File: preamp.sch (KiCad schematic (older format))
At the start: 1 part

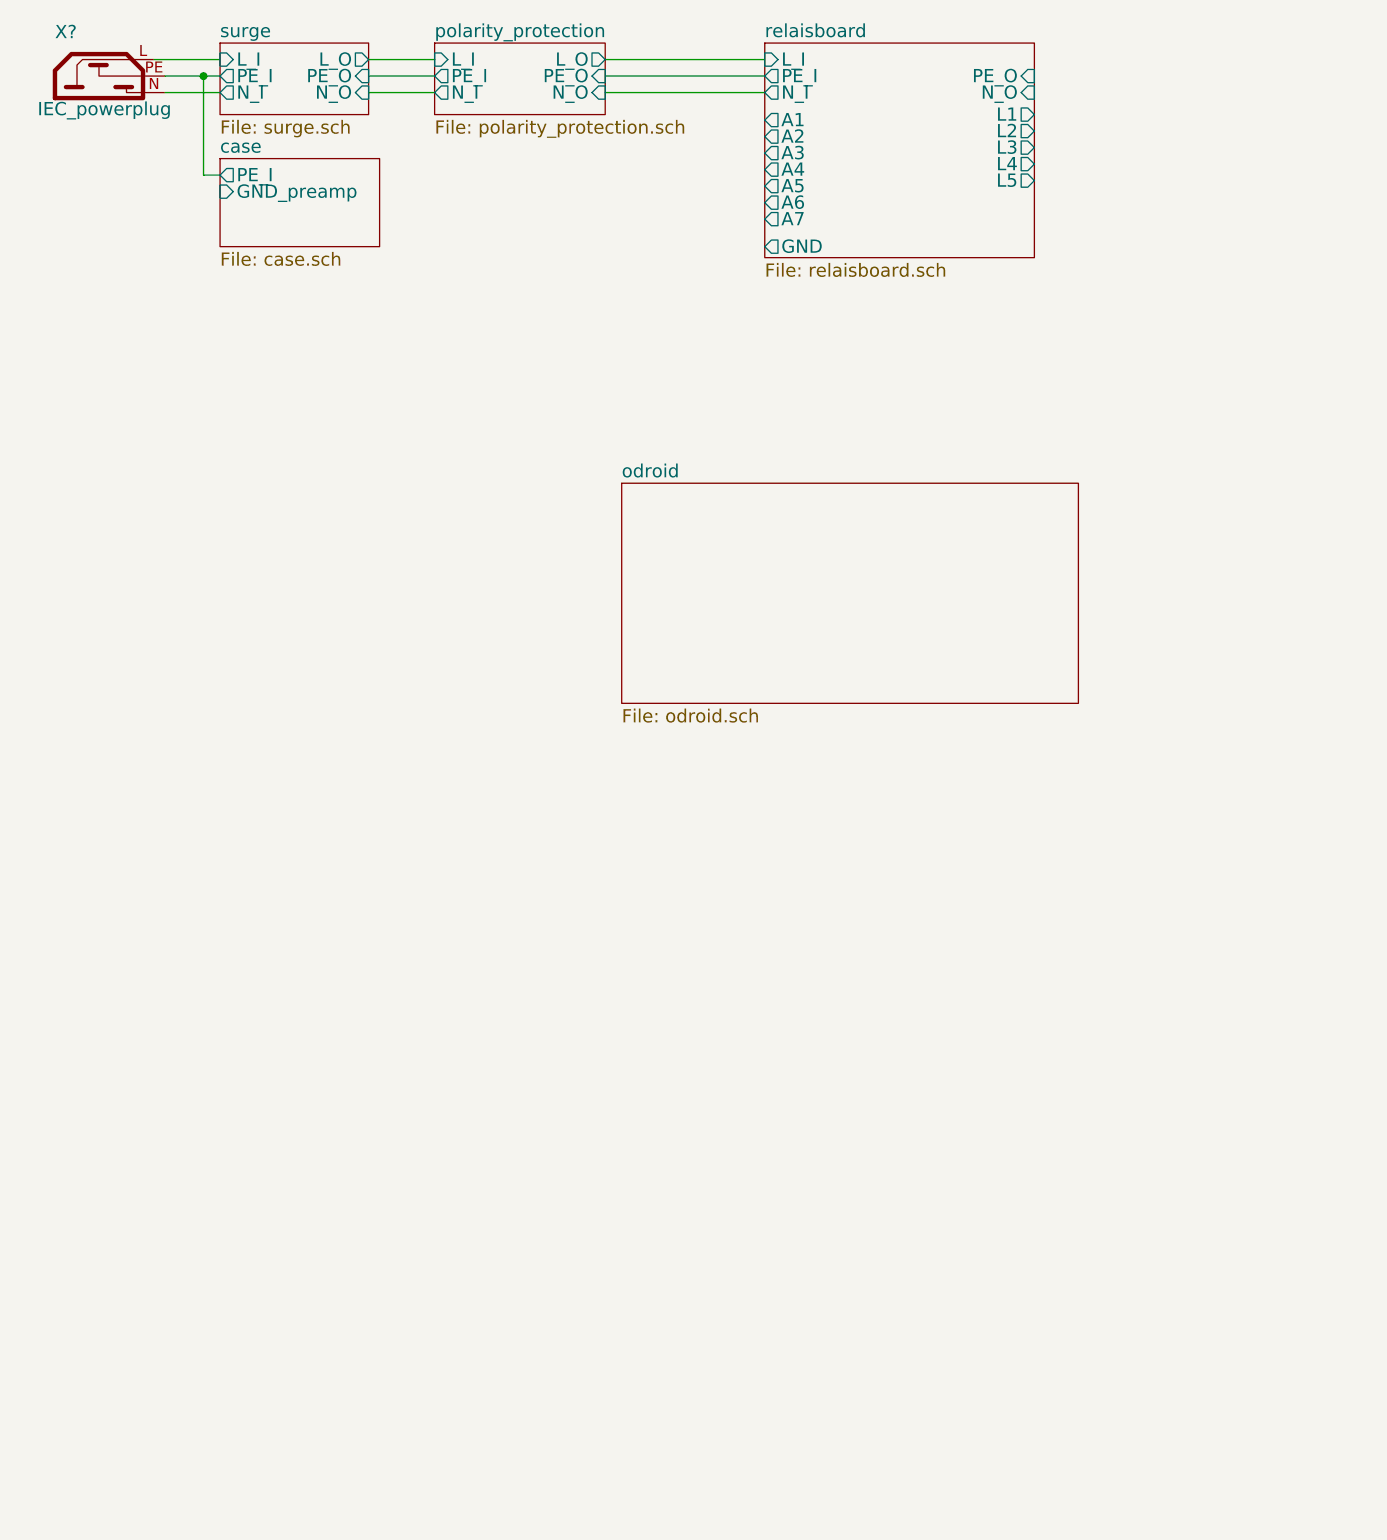
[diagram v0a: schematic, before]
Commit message: toslink reciever and transmitter
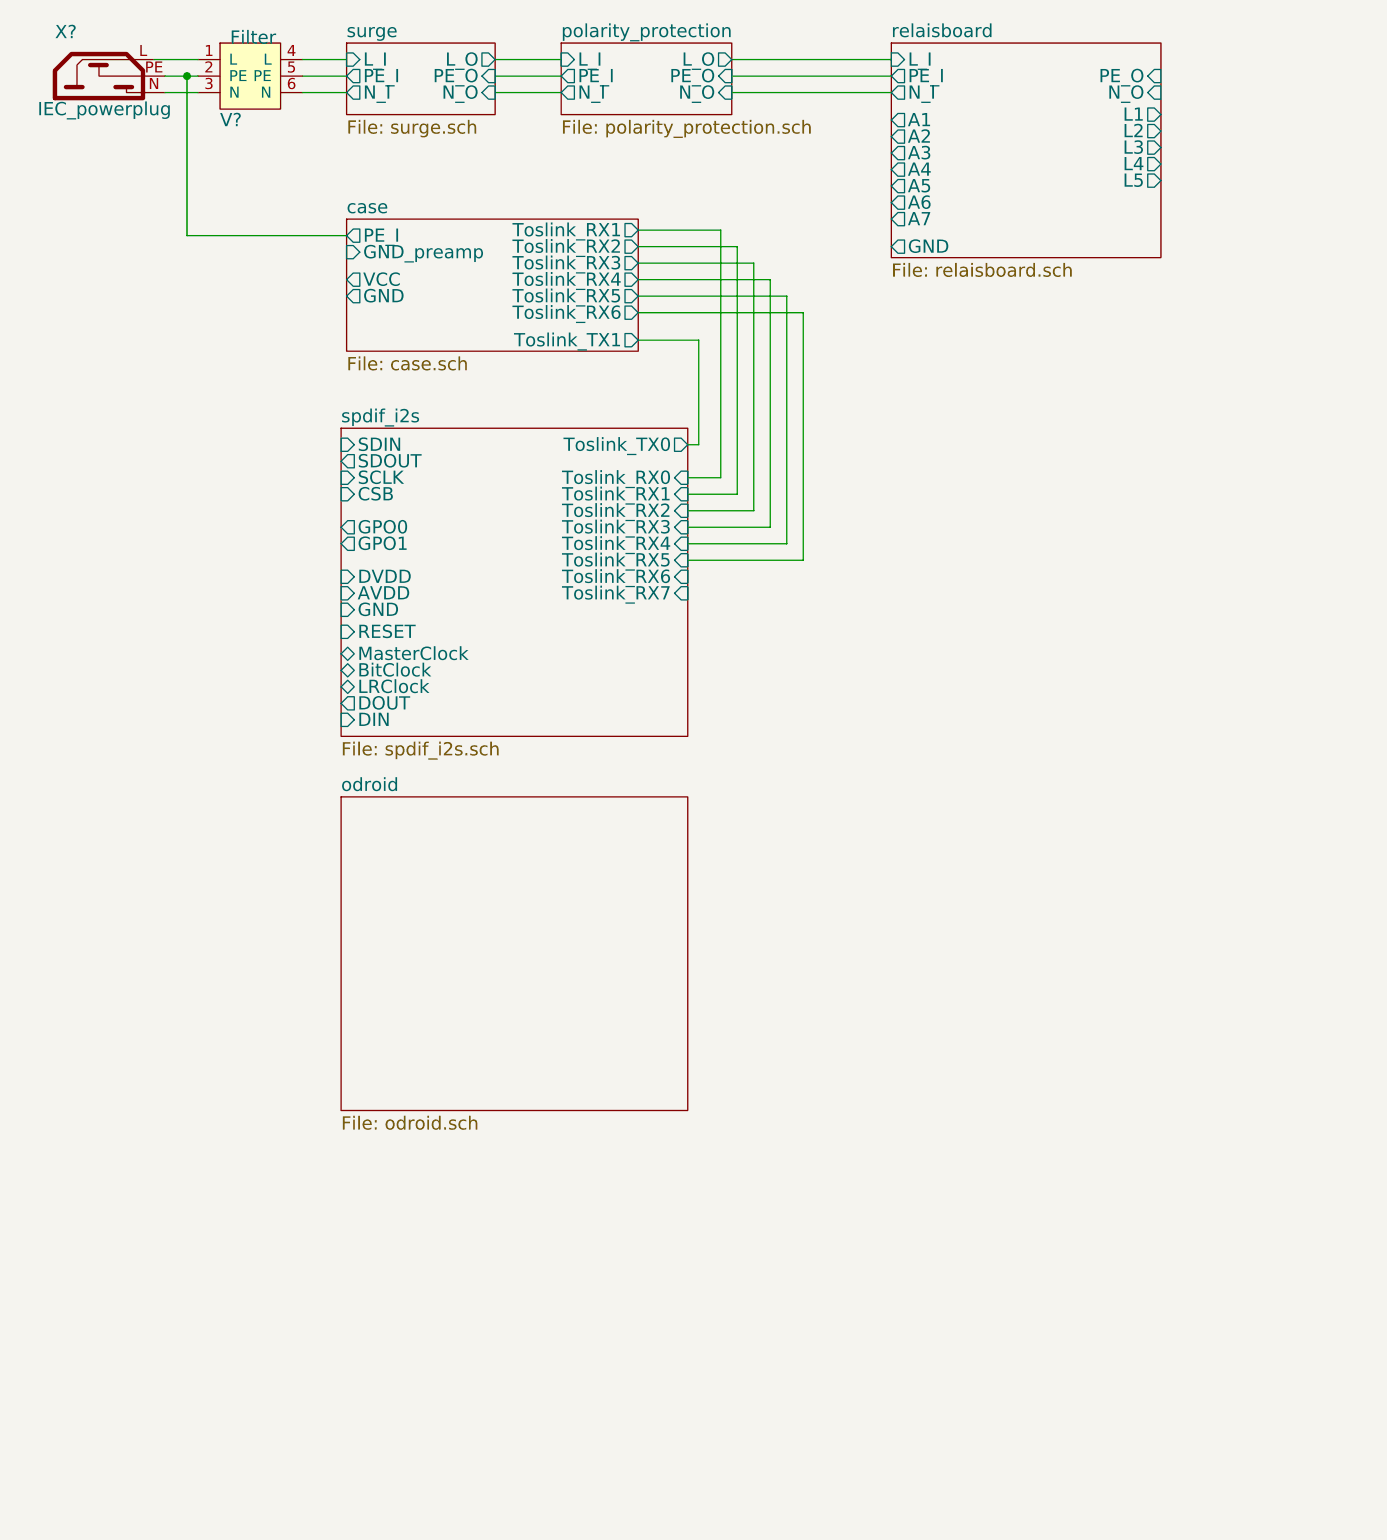
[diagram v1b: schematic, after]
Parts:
- added V?: Filter, symbol Filter
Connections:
- net case/PE_I: now also V?.2 (PE)
- net surge/L_I: now also V?.4 (L); no longer X?.L
- net surge/N_I: now also V?.6 (N); no longer X?.N
- new net: V?.1 (L), X?.L
- new net: V?.3 (N), X?.N
- new net surge/PE_I: V?.5 (PE)
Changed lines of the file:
@@
 $Descr A4 11693 8268
 encoding utf-8
-Sheet 1 6
+Sheet 1 7
 Title ""
 Date ""
@@
 $EndDescr
 $Sheet
-S 1425 825  675  325
+S 2000 825  675  325
 U 5882A13F
 F0 "surge" 60
 F1 "surge.sch" 60
-F2 "L_I" I L 1425 900 60
-F3 "PE_I" O L 1425 975 60
-F4 "N_I" O L 1425 1050 60
-F5 "L_O" O R 2100 900 60
-F6 "PE_O" I R 2100 975 60
-F7 "N_O" I R 2100 1050 60
+F2 "L_I" I L 2000 900 60
+F3 "PE_I" O L 2000 975 60
+F4 "N_I" O L 2000 1050 60
+F5 "L_O" O R 2675 900 60
+F6 "PE_O" I R 2675 975 60
+F7 "N_O" I R 2675 1050 60
 $EndSheet
 $Comp
@@
 	1    0    0    -1
 $EndComp
-Wire Wire Line
-	1125 900  1425 900
-Wire Wire Line
-	1175 975  1425 975
-Wire Wire Line
-	1175 1050 1425 1050
-$Sheet
-S 2400 825  775  325
+$Sheet
+S 2975 825  775  325
 U 58836B99
 F0 "polarity_protection" 60
 F1 "polarity_protection.sch" 60
-F2 "L_I" I L 2400 900 60
-F3 "PE_I" O L 2400 975 60
-F4 "N_I" O L 2400 1050 60
-F5 "L_O" O R 3175 900 60
-F6 "PE_O" I R 3175 975 60
-F7 "N_O" I R 3175 1050 60
-$EndSheet
-Wire Wire Line
-	2100 900  2400 900
-Wire Wire Line
-	2400 975  2100 975
-Wire Wire Line
-	2100 1050 2400 1050
-$Sheet
-S 3900 825  1225 975
+F2 "L_I" I L 2975 900 60
+F3 "PE_I" O L 2975 975 60
+F4 "N_I" O L 2975 1050 60
+F5 "L_O" O R 3750 900 60
+F6 "PE_O" I R 3750 975 60
+F7 "N_O" I R 3750 1050 60
+$EndSheet
+Wire Wire Line
+	2675 900  2975 900
+Wire Wire Line
+	2975 975  2675 975
+Wire Wire Line
+	2675 1050 2975 1050
+$Sheet
+S 4475 825  1225 975
 U 58838AD0
 F0 "relaisboard" 60
 F1 "relaisboard.sch" 60
-F2 "L_I" I L 3900 900 60
-F3 "PE_I" O L 3900 975 60
-F4 "N_I" O L 3900 1050 60
-F5 "PE_O" I R 5125 975 60
-F6 "N_O" I R 5125 1050 60
-F7 "L1" O R 5125 1150 60
-F8 "L2" O R 5125 1225 60
-F9 "L3" O R 5125 1300 60
-F10 "L4" O R 5125 1375 60
-F11 "L5" O R 5125 1450 60
-F12 "GND" O L 3900 1750 60
-F13 "A1" O L 3900 1175 60
-F14 "A2" O L 3900 1250 60
-F15 "A3" O L 3900 1325 60
-F16 "A4" O L 3900 1400 60
-F17 "A5" O L 3900 1475 60
-F18 "A6" O L 3900 1550 60
-F19 "A7" O L 3900 1625 60
-$EndSheet
-Wire Wire Line
-	3900 900  3175 900
-Wire Wire Line
-	3175 975  3900 975
-Wire Wire Line
-	3900 1050 3175 1050
-$Sheet
-S 1425 1350 725  400
+F2 "L_I" I L 4475 900 60
+F3 "PE_I" O L 4475 975 60
+F4 "N_I" O L 4475 1050 60
+F5 "PE_O" I R 5700 975 60
+F6 "N_O" I R 5700 1050 60
+F7 "L1" O R 5700 1150 60
+F8 "L2" O R 5700 1225 60
+F9 "L3" O R 5700 1300 60
+F10 "L4" O R 5700 1375 60
+F11 "L5" O R 5700 1450 60
+F12 "GND" O L 4475 1750 60
+F13 "A1" O L 4475 1175 60
+F14 "A2" O L 4475 1250 60
+F15 "A3" O L 4475 1325 60
+F16 "A4" O L 4475 1400 60
+F17 "A5" O L 4475 1475 60
+F18 "A6" O L 4475 1550 60
+F19 "A7" O L 4475 1625 60
+$EndSheet
+Wire Wire Line
+	4475 900  3750 900
+Wire Wire Line
+	3750 975  4475 975
+Wire Wire Line
+	4475 1050 3750 1050
+$Sheet
+S 2000 1625 1325 600
 U 5883E969
 F0 "case" 60
 F1 "case.sch" 60
-F2 "GND_preamp" I L 1425 1500 60
-F3 "PE_I" O L 1425 1425 60
-$EndSheet
-Wire Wire Line
-	1425 1425 1350 1425
-Wire Wire Line
-	1350 1425 1350 975
-Connection ~ 1350 975
-$Sheet
-S 3250 2825 2075 1000
+F2 "GND_preamp" I L 2000 1775 60
+F3 "PE_I" O L 2000 1700 60
+F4 "GND" O L 2000 1975 60
+F5 "VCC" O L 2000 1900 60
+F6 "Toslink_RX1" O R 3325 1675 60
+F7 "Toslink_RX2" O R 3325 1750 60
+F8 "Toslink_RX3" O R 3325 1825 60
+F9 "Toslink_RX4" O R 3325 1900 60
+F10 "Toslink_RX5" O R 3325 1975 60
+F11 "Toslink_RX6" O R 3325 2050 60
+F12 "Toslink_TX1" O R 3325 2175 60
+$EndSheet
+$Sheet
+S 1975 4250 1575 1425
 U 58843538
 F0 "odroid" 60
 F1 "odroid.sch" 60
 $EndSheet
+$Sheet
+S 1975 2575 1575 1400
+U 5885CB61
+F0 "spdif_i2s" 60
+F1 "spdif_i2s.sch" 60
+F2 "RESET" I L 1975 3500 60
+F3 "SDOUT" O L 1975 2725 60
+F4 "SDIN" I L 1975 2650 60
+F5 "SCLK" I L 1975 2800 60
+F6 "CSB" I L 1975 2875 60
+F7 "GPO1" O L 1975 3100 60
+F8 "GPO0" O L 1975 3025 60
+F9 "Toslink_TX0" O R 3550 2650 60
+F10 "Toslink_RX7" I R 3550 3325 60
+F11 "Toslink_RX6" I R 3550 3250 60
+F12 "Toslink_RX5" I R 3550 3175 60
+F13 "Toslink_RX4" I R 3550 3100 60
+F14 "Toslink_RX3" I R 3550 3025 60
+F15 "Toslink_RX2" I R 3550 2950 60
+F16 "Toslink_RX1" I R 3550 2875 60
+F17 "Toslink_RX0" I R 3550 2800 60
+F18 "MasterClock" B L 1975 3600 60
+F19 "BitClock" B L 1975 3675 60
+F20 "LRClock" B L 1975 3750 60
+F21 "DOUT" O L 1975 3825 60
+F22 "DIN" I L 1975 3900 60
+F23 "DVDD" I L 1975 3250 60
+F24 "AVDD" I L 1975 3325 60
+F25 "GND" I L 1975 3400 60
+$EndSheet
+$Comp
+L Filter V?
+U 1 1 588AF3AE
+P 1575 950
+F 0 "V?" H 1475 725 60  0000 C CNN
+F 1 "Filter" H 1575 1100 60  0000 C CNN
+F 2 "" H 1575 950 60  0001 C CNN
+F 3 "" H 1575 950 60  0001 C CNN
+	1    1575 950
+	1    0    0    -1
+$EndComp
+Wire Wire Line
+	1325 900  1125 900
+Wire Wire Line
+	1175 975  1325 975
+Wire Wire Line
+	1175 1050 1325 1050
+Wire Wire Line
+	1800 900  2000 900
+Wire Wire Line
+	1800 975  2000 975
+Wire Wire Line
+	1800 1050 2000 1050
+Wire Wire Line
+	2000 1700 1275 1700
+Wire Wire Line
+	1275 1700 1275 975
+Connection ~ 1275 975
+Wire Wire Line
+	3325 2175 3600 2175
+Wire Wire Line
+	3600 2175 3600 2650
+Wire Wire Line
+	3600 2650 3550 2650
+Wire Wire Line
+	3550 2800 3700 2800
+Wire Wire Line
+	3700 2800 3700 1675
+Wire Wire Line
+	3700 1675 3325 1675
+Wire Wire Line
+	3550 2875 3775 2875
+Wire Wire Line
+	3775 2875 3775 1750
+Wire Wire Line
+	3775 1750 3325 1750
+Wire Wire Line
+	3325 1825 3850 1825
+Wire Wire Line
+	3850 1825 3850 2950
+Wire Wire Line
+	3850 2950 3550 2950
+Wire Wire Line
+	3550 3025 3925 3025
+Wire Wire Line
+	3925 3025 3925 1900
+Wire Wire Line
+	3925 1900 3325 1900
+Wire Wire Line
+	3325 1975 4000 1975
+Wire Wire Line
+	4000 1975 4000 3100
+Wire Wire Line
+	4000 3100 3550 3100
+Wire Wire Line
+	3550 3175 4075 3175
+Wire Wire Line
+	4075 3175 4075 2050
+Wire Wire Line
+	4075 2050 3325 2050
 $EndSCHEMATC

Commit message: Odroid
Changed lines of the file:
@@
 	2675 1050 2975 1050
 $Sheet
-S 4475 825  1225 975
+S 4750 825  925  725
 U 58838AD0
 F0 "relaisboard" 60
 F1 "relaisboard.sch" 60
-F2 "L_I" I L 4475 900 60
-F3 "PE_I" O L 4475 975 60
-F4 "N_I" O L 4475 1050 60
-F5 "PE_O" I R 5700 975 60
-F6 "N_O" I R 5700 1050 60
-F7 "L1" O R 5700 1150 60
-F8 "L2" O R 5700 1225 60
-F9 "L3" O R 5700 1300 60
-F10 "L4" O R 5700 1375 60
-F11 "L5" O R 5700 1450 60
-F12 "GND" O L 4475 1750 60
-F13 "A1" O L 4475 1175 60
-F14 "A2" O L 4475 1250 60
-F15 "A3" O L 4475 1325 60
-F16 "A4" O L 4475 1400 60
-F17 "A5" O L 4475 1475 60
-F18 "A6" O L 4475 1550 60
-F19 "A7" O L 4475 1625 60
+F2 "L_I" I L 4750 900 60
+F3 "PE_I" O L 4750 975 60
+F4 "N_I" O L 4750 1050 60
+F5 "PE_O" I R 5675 975 60
+F6 "N_O" I R 5675 1050 60
+F7 "L1" O R 5675 1150 60
+F8 "L2" O R 5675 1225 60
+F9 "L3" O R 5675 1300 60
+F10 "L4" O R 5675 1375 60
+F11 "L5" O R 5675 1450 60
+F12 "GND" O L 4750 1250 60
+F13 "VCC" I L 4750 1175 60
+F14 "SCL" I L 4750 1350 60
+F15 "SDA" B L 4750 1425 60
 $EndSheet
 Wire Wire Line
-	4475 900  3750 900
+	4750 900  3750 900
 Wire Wire Line
-	3750 975  4475 975
+	3750 975  4750 975
 Wire Wire Line
-	4475 1050 3750 1050
+	4750 1050 3750 1050
 $Sheet
-S 2000 1625 1325 600
+S 2000 1625 1325 925
 U 5883E969
 F0 "case" 60
@@
 $EndSheet
 $Sheet
-S 1975 4250 1575 1425
+S 1975 4500 1575 1425
 U 58843538
 F0 "odroid" 60
 F1 "odroid.sch" 60
+F2 "SCL" O R 3550 4550 60
+F3 "SDA" B R 3550 4625 60
 $EndSheet
 $Sheet
-S 1975 2575 1575 1400
+S 1975 2825 1575 1400
 U 5885CB61
 F0 "spdif_i2s" 60
 F1 "spdif_i2s.sch" 60
-F2 "RESET" I L 1975 3500 60
-F3 "SDOUT" O L 1975 2725 60
-F4 "SDIN" I L 1975 2650 60
-F5 "SCLK" I L 1975 2800 60
-F6 "CSB" I L 1975 2875 60
-F7 "GPO1" O L 1975 3100 60
-F8 "GPO0" O L 1975 3025 60
-F9 "Toslink_TX0" O R 3550 2650 60
-F10 "Toslink_RX7" I R 3550 3325 60
-F11 "Toslink_RX6" I R 3550 3250 60
-F12 "Toslink_RX5" I R 3550 3175 60
-F13 "Toslink_RX4" I R 3550 3100 60
-F14 "Toslink_RX3" I R 3550 3025 60
-F15 "Toslink_RX2" I R 3550 2950 60
-F16 "Toslink_RX1" I R 3550 2875 60
-F17 "Toslink_RX0" I R 3550 2800 60
-F18 "MasterClock" B L 1975 3600 60
-F19 "BitClock" B L 1975 3675 60
-F20 "LRClock" B L 1975 3750 60
-F21 "DOUT" O L 1975 3825 60
-F22 "DIN" I L 1975 3900 60
-F23 "DVDD" I L 1975 3250 60
-F24 "AVDD" I L 1975 3325 60
-F25 "GND" I L 1975 3400 60
+F2 "RESET" I L 1975 3750 60
+F3 "SDOUT" O L 1975 2975 60
+F4 "SDIN" I L 1975 2900 60
+F5 "SCLK" I L 1975 3050 60
+F6 "CSB" I L 1975 3125 60
+F7 "GPO1" O L 1975 3350 60
+F8 "GPO0" O L 1975 3275 60
+F9 "Toslink_TX0" O R 3550 2900 60
+F10 "Toslink_RX7" I R 3550 3575 60
+F11 "Toslink_RX6" I R 3550 3500 60
+F12 "Toslink_RX5" I R 3550 3425 60
+F13 "Toslink_RX4" I R 3550 3350 60
+F14 "Toslink_RX3" I R 3550 3275 60
+F15 "Toslink_RX2" I R 3550 3200 60
+F16 "Toslink_RX1" I R 3550 3125 60
+F17 "Toslink_RX0" I R 3550 3050 60
+F18 "MasterClock" B L 1975 3850 60
+F19 "BitClock" B L 1975 3925 60
+F20 "LRClock" B L 1975 4000 60
+F21 "DOUT" O L 1975 4075 60
+F22 "DIN" I L 1975 4150 60
+F23 "DVDD" I L 1975 3500 60
+F24 "AVDD" I L 1975 3575 60
+F25 "GND" I L 1975 3650 60
 $EndSheet
 $Comp
@@
 	1325 900  1125 900
 Wire Wire Line
-	1175 975  1325 975
+	1175 975  1275 975
+Wire Wire Line
+	1275 975  1325 975
 Wire Wire Line
 	1175 1050 1325 1050
@@
 Connection ~ 1275 975
 Wire Wire Line
-	3325 2175 3600 2175
+	3325 2175 3625 2175
 Wire Wire Line
-	3600 2175 3600 2650
+	3625 2175 3625 2900
 Wire Wire Line
-	3600 2650 3550 2650
+	3625 2900 3550 2900
 Wire Wire Line
-	3550 2800 3700 2800
+	3550 3050 3800 3050
 Wire Wire Line
-	3700 2800 3700 1675
+	3800 3050 3800 1675
 Wire Wire Line
-	3700 1675 3325 1675
+	3800 1675 3325 1675
 Wire Wire Line
-	3550 2875 3775 2875
+	3550 3125 3875 3125
 Wire Wire Line
-	3775 2875 3775 1750
+	3875 3125 3875 1750
 Wire Wire Line
-	3775 1750 3325 1750
+	3875 1750 3325 1750
 Wire Wire Line
-	3325 1825 3850 1825
+	3325 1825 3950 1825
 Wire Wire Line
-	3850 1825 3850 2950
+	3950 1825 3950 3200
 Wire Wire Line
-	3850 2950 3550 2950
+	3950 3200 3550 3200
 Wire Wire Line
-	3550 3025 3925 3025
+	3550 3275 4025 3275
 Wire Wire Line
-	3925 3025 3925 1900
+	4025 3275 4025 1900
 Wire Wire Line
-	3925 1900 3325 1900
+	4025 1900 3325 1900
 Wire Wire Line
-	3325 1975 4000 1975
+	3325 1975 4100 1975
 Wire Wire Line
-	4000 1975 4000 3100
+	4100 1975 4100 3350
 Wire Wire Line
-	4000 3100 3550 3100
+	4100 3350 3550 3350
 Wire Wire Line
-	3550 3175 4075 3175
+	3550 3425 4175 3425
 Wire Wire Line
-	4075 3175 4075 2050
+	4175 3425 4175 2050
 Wire Wire Line
-	4075 2050 3325 2050
+	4175 2050 3325 2050
+Wire Wire Line
+	3550 4550 4425 4550
+Wire Wire Line
+	4425 4550 4425 1350
+Wire Wire Line
+	4425 1350 4750 1350
+Wire Wire Line
+	3550 4625 4500 4625
+Wire Wire Line
+	4500 4625 4500 1425
+Wire Wire Line
+	4500 1425 4750 1425
 $EndSCHEMATC
